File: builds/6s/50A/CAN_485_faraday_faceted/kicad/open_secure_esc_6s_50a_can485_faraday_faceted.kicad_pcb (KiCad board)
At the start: 4 copper layers, 49 x 89.5 mm, 65 parts, among them J1 SolderPad_1x04_SMD_P1.27mm_Pr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, J2 SolderPad_1x02_SMD_P2.54mm, J3 SolderPad_1x02_SMD_P2.54mm, J4A SolderWirePad_1x01_SMD_5x10mm, J4B SolderWirePad_1x01_SMD_5x10mm, J4C SolderWirePad_1x01_SMD_5x10mm, J5A SolderWire-6sqmm_1x01_D3.5mm_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, J5B SolderWire-6sqmm_1x01_D3.5mm_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, Q1 Toshiba_2-5W1A_SOP-Advance-N_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, Q2 Toshiba_2-5W1A_SOP-Advance-N_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, Q3 Toshiba_2-5W1A_SOP-Advance-N_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, Q4 Toshiba_2-5W1A_SOP-Advance-N_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, Q5 Toshiba_2-5W1A_SOP-Advance-N_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, Q6 Toshiba_2-5W1A_SOP-Advance-N_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, U1 LQFP-64_10x10mm_P0.5mm, U2 Infineon_PG-USON-10-2-4_3x3mm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, U3 SOIC-20W_7.5x12.8mm_P1.27mm, U4 SOIC-20W_7.5x12.8mm_P1.27mm, U5 TI_RTA0040B_WQFN-40_6x6mm_P0.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, U6 SOIC-8_3.9x4.9mm_P1.27mm, U7 SOIC-8_3.9x4.9mm_P1.27mm, U8 SOIC-8_3.9x4.9mm_P1.27mm

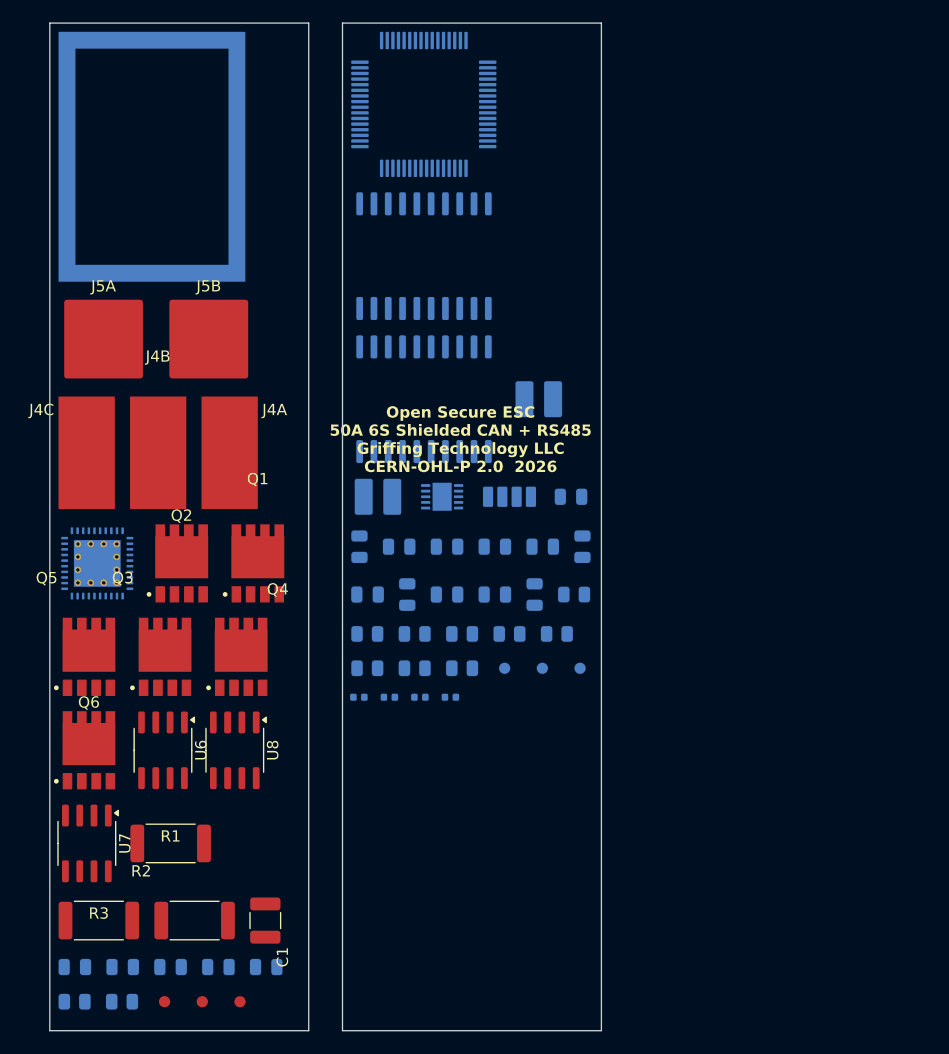
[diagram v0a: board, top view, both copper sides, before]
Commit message: WIP: stage RHB on the 4th board; fix the 18 FET drain ERC errors
NOTE ON CAN_485_faraday_faceted: this board was open in a live KiCad
GUI session for manual component repositioning (compacting the
layout) while the rest of this branch's work was done, so it was
skipped until the repo owner closed that session. It's now released
and this commit adds the RHB footprint to it -- same treatment as the
other three boards (Package_DFN_QFN:Texas_RHB0032E_VQFN-32-1EP_5x5mm
replacing the stale LQFP-64, every pad wired to its correct net,
staged off-board clear of the board outline for manual placement).

IMPORTANT: the repo owner's manual compaction on this specific board
is IN PROGRESS, not finished ("it needs more work" -- their words).
The committed .kicad_pcb is a snapshot of that in-progress repositioning
plus the staged RHB addition, not a settled layout. Don't treat its
current component placement as final, and don't run any placement
generator against it -- this repo's own rule is never to regenerate a
board after manual packing, and that applies here same as anywhere
else. `kicad-cli pcb drc` confirms the RHB addition itself introduced
no new violations on top of whatever compaction state was already
there (63 violations / 182 unconnected before and after).

Also fixes the 18 pre-existing pin_not_connected ERC errors on
CAN_485_faraday_sameend (Q1-Q6 TPHR8504PL drain pins 5/6/7) flagged by
CI's KiCad ERC/DRC check -- these are pure schematic-connectivity gaps,
independent of any board's component placement, so fixed here rather
than left for after the layout work. Root cause: the FET symbol's
redundant parallel drain pins (5-8, all electrically the same drain
per symbols/specs/TPHR8504PL.json) were left unwired when the symbol
was expanded from an older 3-pin stub to the verified 8-pin version;
only pin 8 carried the real net. Fixed with 3 short wire segments per
FET bussing pins 5-6-7-8 together, each one verified against a
netlist re-export before being trusted -- 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
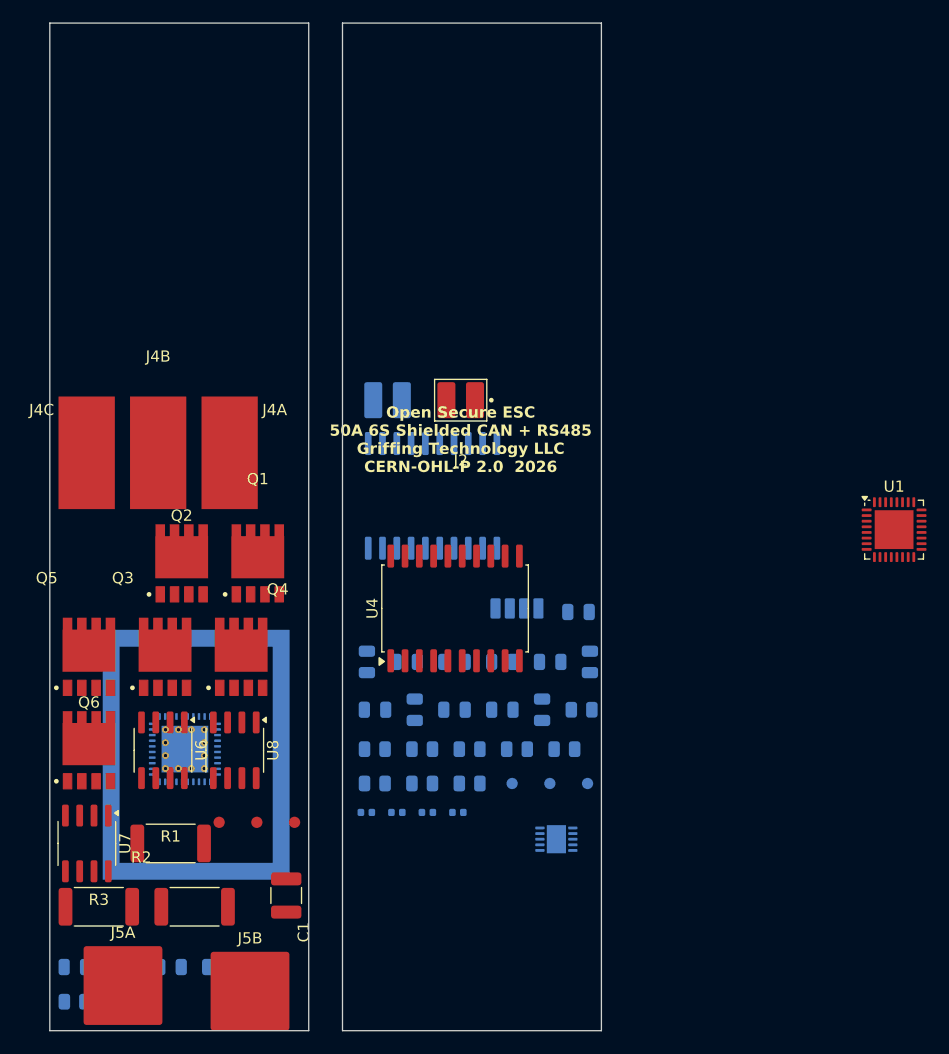
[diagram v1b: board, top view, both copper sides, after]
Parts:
- J2, U4: moved to F.Cu
- U1: value LQFP-64_10x10mm_P0.5mm -> MSPM0G3518_Q1_RHB; footprint LQFP-64_10x10mm_P0.5mm -> Package_DFN_QFN:Texas_RHB0032E_VQFN-32-1EP_5x5mm_P0.5mm_EP3.45x3.45mm; moved to F.Cu
- moved J5B 58.0 mm to (17.8, 86.0)
- moved J5A 57.5 mm to (6.50, 85.5)
- moved U1 56.3 mm to (75.0, 45.0), turned to 0 degrees
- moved SH1 53.3 mm to (13.0, 65.0)
- moved U2 32.1 mm to (45.0, 72.5)
- moved U4 31.4 mm to (36.0, 52.0)
- moved U5 18.2 mm to (12.0, 64.5)
- moved FID1 16.7 mm to (18.4, 71.0)
- moved FID2 16.7 mm to (15.0, 71.0)
- moved FID3 16.7 mm to (21.7, 71.0)
- moved FB1 10.3 mm to (36.2, 70.1)
- moved FB2 10.3 mm to (30.8, 70.1)
- moved FB3 10.3 mm to (28.1, 70.1)
- moved FB4 10.3 mm to (33.5, 70.1)
- moved C10 10.3 mm to (47.0, 52.3)
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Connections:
- U1 pad 1: Net-(U1-GD_SPI_CS) -> Net-(U1-RS485_TXD)
- U1 pad 10: (no net) -> RS485_DE_RE
- U1 pad 12: Net-(J1-Pin_1) -> Net-(U1-PWM_AH)
- U1 pad 13: Net-(J1-Pin_2) -> Net-(U1-PWM_AL)
- U1 pad 14: (no net) -> Net-(U1-PWM_CH)
- U1 pad 15: (no net) -> Net-(U1-PWM_CL)
- U1 pad 16: (no net) -> Net-(U1-CAN_TX)
- U1 pad 17: VBUS_SENSE -> Net-(U1-CAN_RX)
- U1 pad 18: (no net) -> SE_RST
- U1 pad 19: (no net) -> SE_I2C_SCL
- U1 pad 2: GD_SPI_MISO -> Net-(U1-RS485_RXD)
- U1 pad 20: (no net) -> GD_SPI_MISO
- U1 pad 21: (no net) -> Net-(U1-GD_SPI_SCK)
- U1 pad 22: (no net) -> Net-(U1-GD_SPI_MOSI)
- U1 pad 23: (no net) -> Net-(J1-Pin_1)
- U1 pad 24: ADC_IV -> Net-(J1-Pin_2)
- U1 pad 25: ADC_IU -> VBUS_SENSE
- U1 pad 26: ADC_IW -> (no net)
- U1 pad 27: (no net) -> ADC_IV
- U1 pad 28: (no net) -> ADC_IU
- U1 pad 29: (no net) -> ADC_IW
- U1 pad 3: Net-(U1-GD_SPI_MOSI) -> NRST
- U1 pad 30: Net-(U1-CAN_TX) -> (no net)
- U1 pad 31: Net-(U1-CAN_RX) -> (no net)
- U1 pad 33: Net-(U1-RS485_TXD) -> (no net)
- U1 pad 4: Net-(U1-GD_SPI_SCK) -> 3V3
- U1 pad 5: (no net) -> GND
- U1 pad 6: (no net) -> Net-(U1-GD_SPI_CS)
- U1 pad 7: SE_RST -> Net-(U1-PWM_BH)
- U1 pad 8: SE_I2C_SCL -> Net-(U1-PWM_BL)
